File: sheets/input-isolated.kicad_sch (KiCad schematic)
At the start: 10 parts, among them U9 HCPL2630SDVM

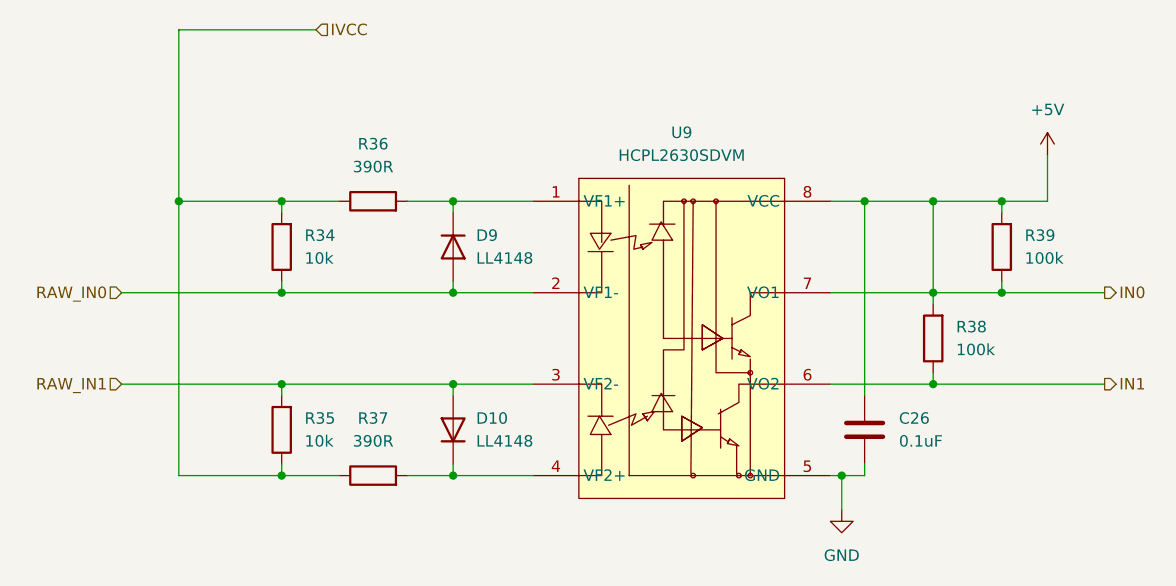
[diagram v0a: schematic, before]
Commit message: add mcu module + position components
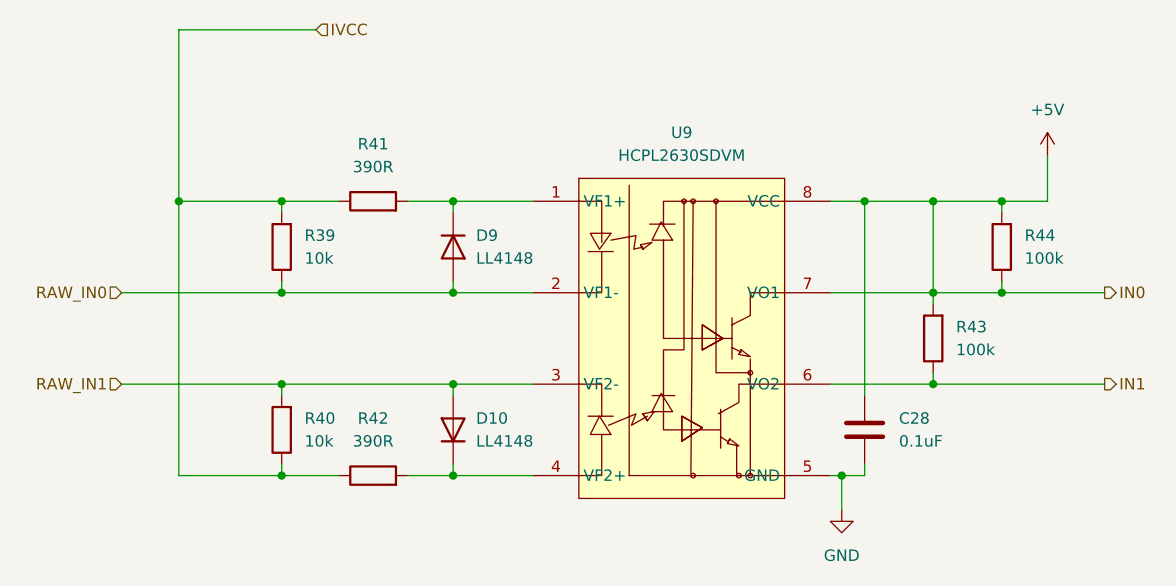
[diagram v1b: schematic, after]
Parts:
- renumbered C26 to C28, R34 to R39, R35 to R40, R36 to R41, R37 to R42, R38 to R43, R39 to R44

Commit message: Updated MCU to MCU module + set SMD comp. footprints
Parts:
- C28: footprint (none) -> Capacitor_SMD:C_0603_1608Metric
- R39, R40, R41, R42, R43, R44: footprint (none) -> Resistor_SMD:R_0603_1608Metric
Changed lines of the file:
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@@
 			)
 		)
-		(property "Footprint" ""
+		(property "Footprint" "Capacitor_SMD:C_0603_1608Metric"
 			(at 176.2252 107.95 0)
 			(effects
@@
 			)
 		)
-		(property "Footprint" ""
+		(property "Footprint" "Resistor_SMD:R_0603_1608Metric"
 			(at 112.268 83.82 90)
 			(effects
@@
 			)
 		)
-		(property "Footprint" ""
+		(property "Footprint" "Resistor_SMD:R_0603_1608Metric"
 			(at 120.65 80.518 90)
 			(effects
@@
 			)
 		)
-		(property "Footprint" ""
+		(property "Footprint" "Resistor_SMD:R_0603_1608Metric"
 			(at 184.658 93.98 90)
 			(effects
@@
 			)
 		)
-		(property "Footprint" ""
+		(property "Footprint" "Resistor_SMD:R_0603_1608Metric"
 			(at 120.65 110.998 90)
 			(effects
@@
 			)
 		)
-		(property "Footprint" ""
+		(property "Footprint" "Resistor_SMD:R_0603_1608Metric"
 			(at 192.278 83.82 90)
 			(effects
@@
 			)
 		)
-		(property "Footprint" ""
+		(property "Footprint" "Resistor_SMD:R_0603_1608Metric"
 			(at 112.268 104.14 90)
 			(effects

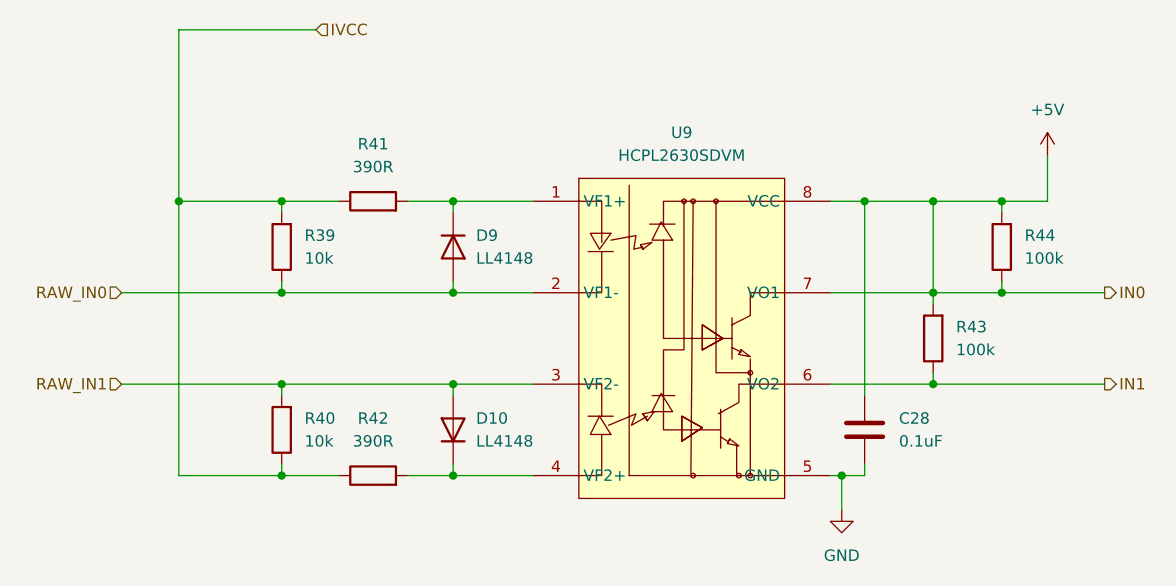
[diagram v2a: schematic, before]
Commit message: add PA an PB ports
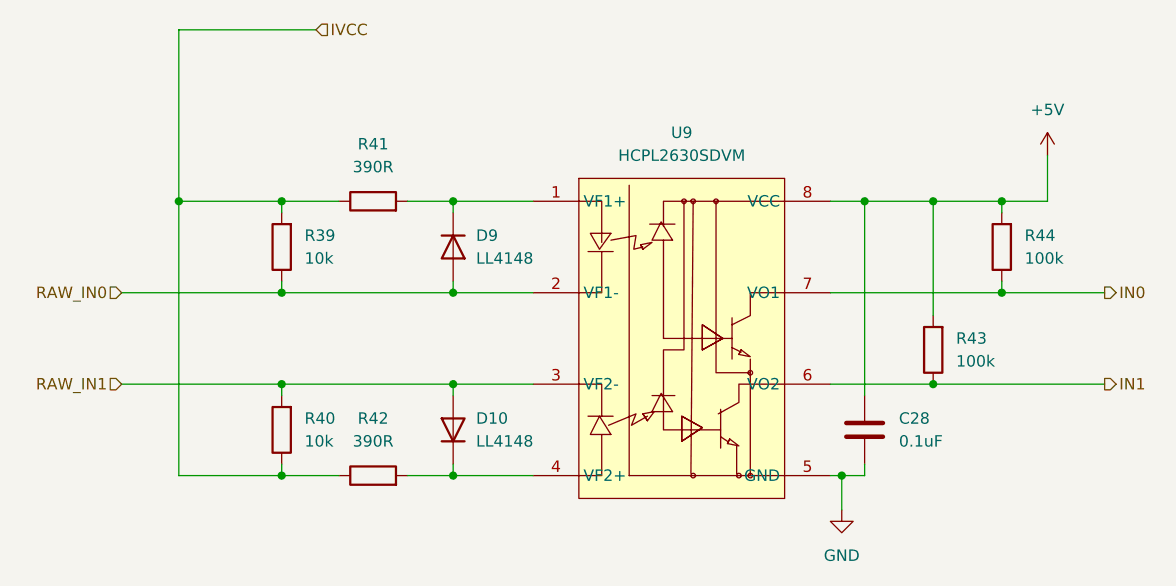
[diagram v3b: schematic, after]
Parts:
- R41, R42: footprint Resistor_SMD:R_0603_1608Metric -> Resistor_SMD:R_1210_3225Metric
- U9: footprint ICs:PDIP-8_L9.6-W6.4-P2.54-LS7.9-BL -> ICs:PDIP8_GW; Manufacturer (none) -> Onsemi; Partnumber (none) -> 6N137SDVM
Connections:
- net +5V: no longer R44.1, U9.7 (VO1)
- new net IN0: R44.1, U9.7 (VO1)
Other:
- moved on the sheet: R43
